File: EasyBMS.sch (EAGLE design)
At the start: 151 parts, among them IC1 LM2596S-5.0_NOPB, IC2 LTC6811IG-1#PBF, IC3 ESP32-S3-WROOM-1-N4R2, IC4 DRV103H, Q10 BSS84LT1G, Q11 BSS84LT1G, Q12 BSS84LT1G, Q13 BSS84LT1G, Q2 BSS84LT1G, Q3 BSS84LT1G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

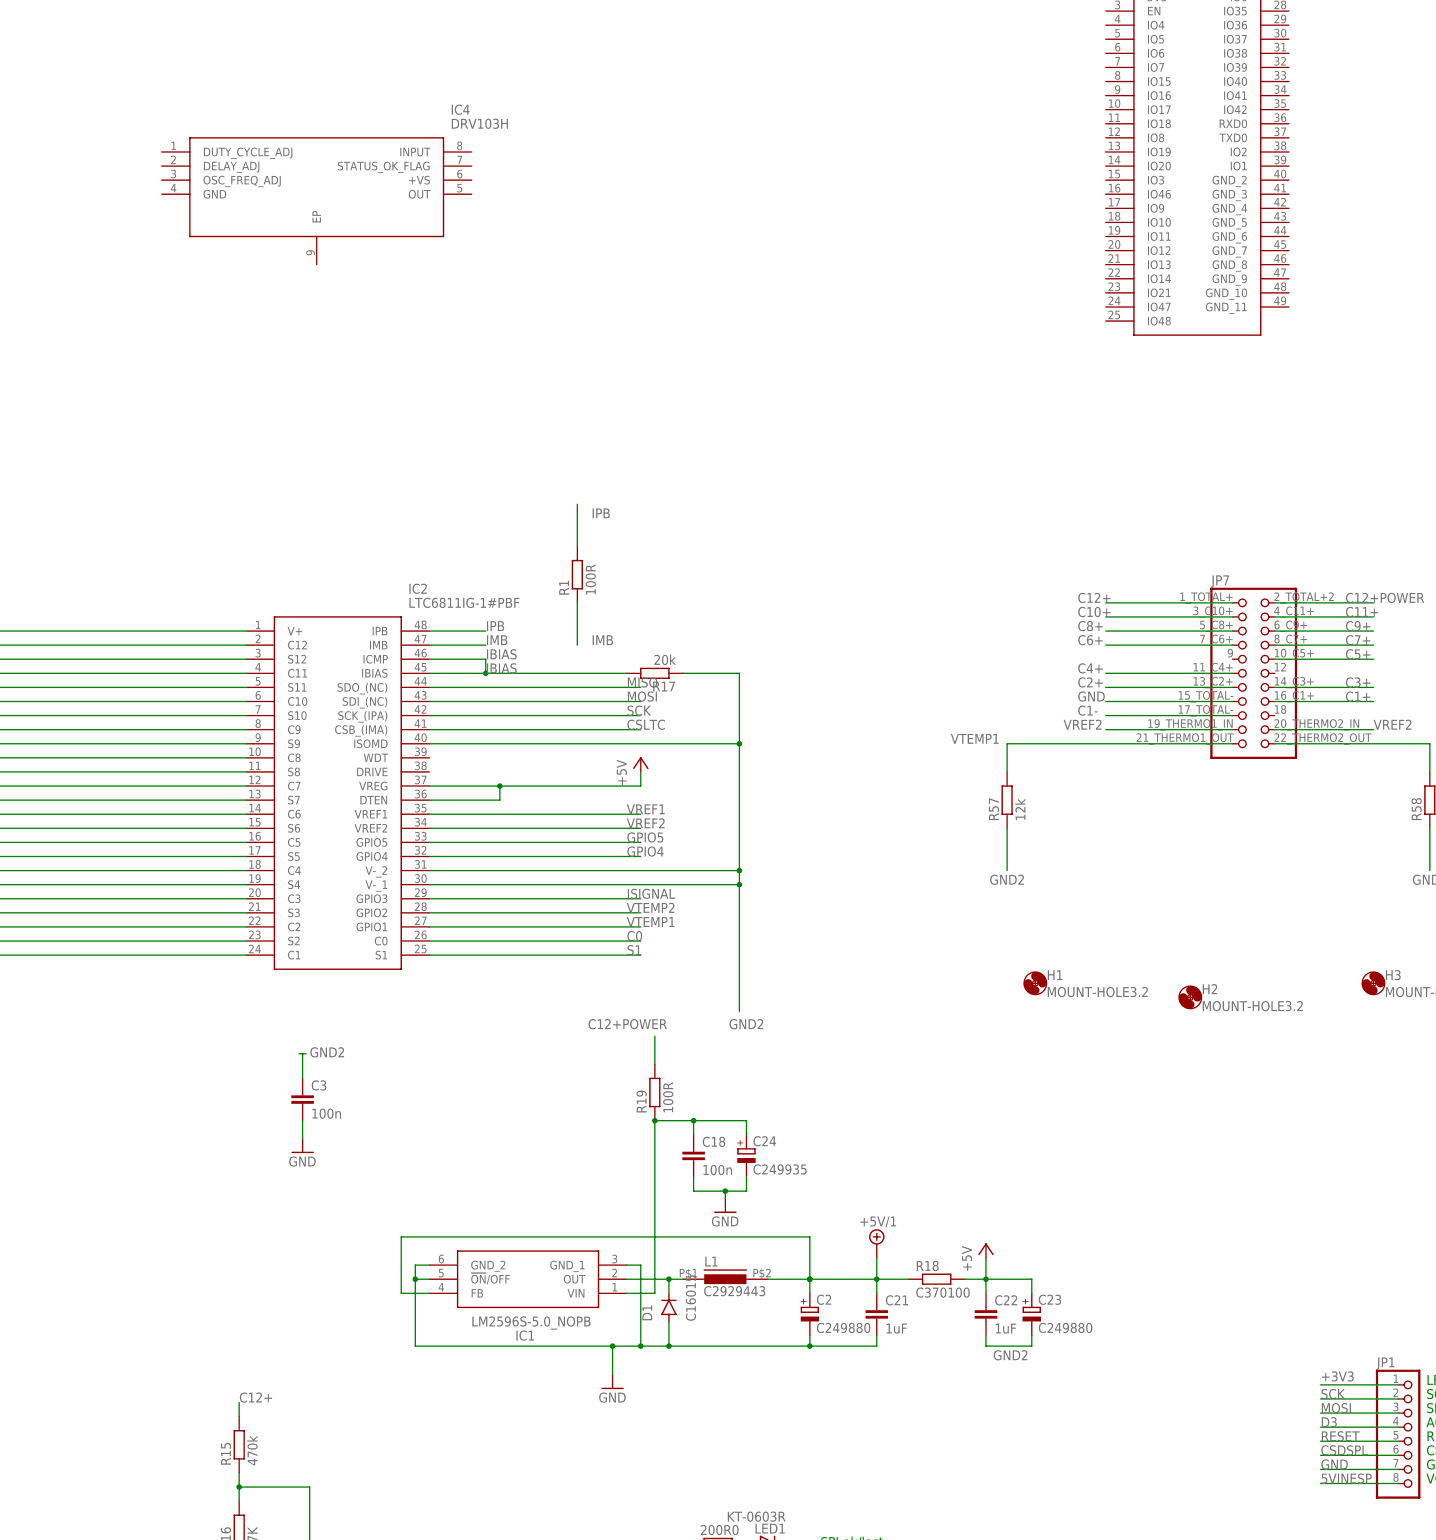
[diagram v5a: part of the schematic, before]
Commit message: new parts for DC DC added
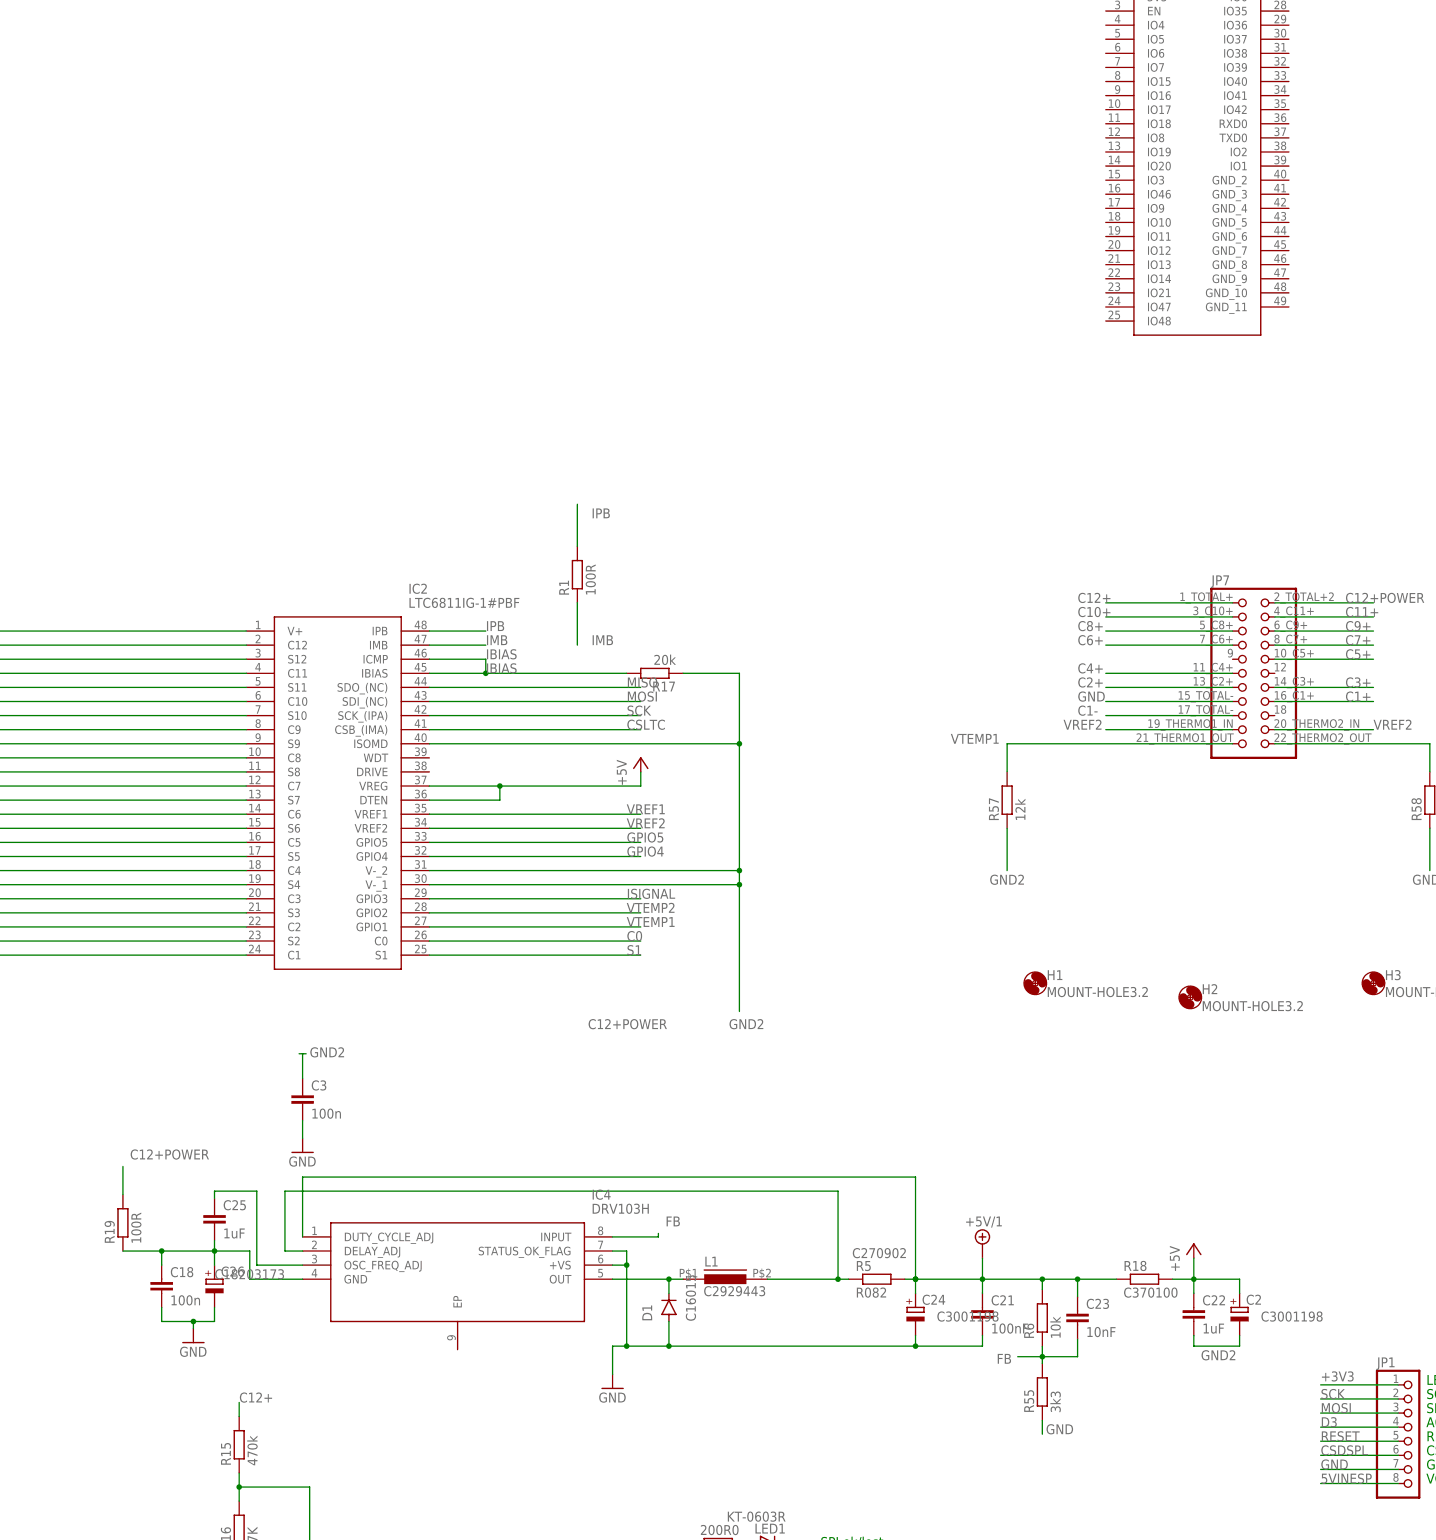
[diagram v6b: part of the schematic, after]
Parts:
- removed IC1: LM2596S-5.0_NOPB, SamacSys_Parts:LM2596S-5.0_NOPB
- added C25: 1uF, rcl:C-EUC1206
- added C26: (no value), rcl:CPOL-EU140CLH-0810
- added R5: R082, rcl:R-EU_R1206
- added R55: 3k3, rcl:R-EU_R0402
- added R6: 10k, rcl:R-EU_R0402
- C2: value C249880 -> (none); device rcl:CPOL-EUUD-8X10 -> rcl:CPOL-EU153CLV-0405; LCSC (none) -> C3001198
- C21: value 1uF -> 100nF; device rcl:C-EUC1206 -> rcl:C-EUC0805
- C23: value C249880 -> 10nF; device rcl:CPOL-EUUD-8X10 -> rcl:C-EUC0402
- C24: value C249935 -> (none); device SamacSys_Parts:VZH471M1JTR-1616 -> rcl:CPOL-EU153CLV-0405; LCSC (none) -> C3001198
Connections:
- new net FB: C23.2, IC4.INPUT, R55.2, R6.1
- new net N$3: C25.1, IC4.OSC_FREQ_ADJ
- new net N$5: IC4.DELAY_ADJ, L1.2, R5.1
- net +5V: now also C2.+; no longer C23.+
- net +5V/1: now also C23.1, C24.+, IC4.DUTY_CYCLE_ADJ, R5.2, R6.2; no longer C2.+, IC1.FB, L1.2
- net GND: now also C26.-, IC4.+VS, IC4.STATUS_OK_FLAG, R55.1; no longer C2.-, IC1.!ON!/OFF, IC1.GND_1, IC1.GND_2
- net GND2: now also C2.-; no longer C23.-
- net N$17: now also IC4.OUT; no longer IC1.OUT
- net N$75: now also C25.2, C26.+, IC4.GND; no longer C24.+, IC1.VIN
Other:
- moved on the sheet: C18, C2, C21, C22, C24, IC4, R18, R19

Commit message: XL7046 properly added
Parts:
- removed C23: 10nF, rcl:C-EUC0402
- removed C25: 1uF, rcl:C-EUC1206
- removed D1: C16015, diode:DIODE-DO214AC
- removed IC4: DRV103H, SamacSys_Parts:DRV103H
- added C27: 1uF, rcl:C-EUC1206
- added D3: C16015, diode:DIODE-DO214AC
- added IC1: XL7046, SamacSys_Parts:XL7046
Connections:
- removed net FB: C23.2, IC4.INPUT, R55.2, R6.1
- removed net N$17: D1.C, IC4.OUT, L1.1
- removed net N$3: C25.1, IC4.OSC_FREQ_ADJ
- removed net N$5: IC4.DELAY_ADJ, L1.2, R5.1
- removed net N$75: C18.1, C25.2, C26.+, IC4.GND, R19.1
- new net N$15: IC1.CSP, L1.2, R5.1
- new net N$25: IC1.FB, R55.2, R6.1
- new net N$6: C27.2, IC1.VC
- new net N$7: D3.C, IC1.SW, L1.1
- new net N$73: C18.1, C26.+, C27.1, IC1.VIN, R19.1
- net +5V/1: now also IC1.CSN; no longer C23.1, IC4.DUTY_CYCLE_ADJ
- net GND: now also D3.A, IC1.GND; no longer D1.A, IC4.+VS, IC4.STATUS_OK_FLAG
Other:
- note added: "LTC BMS Chip"
- note added: "Microcontroller"
- note added: "Pinheader für Display"
- moved on the sheet: C1, C18, C19, C2, C21, C22, C24, C26, C3, C4, D2, JP1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

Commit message: balancer path reworked2
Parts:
- removed U$2: WEMOS-D1-MINI, diy-modules:WEMOS-D1-MINI
- added C25, C29: 10nF, rcl:C-EUC0402
- added D4, D6: (no value), semicon-smd-ipc:D-MLL-34
- added Q14, Q16: C8547, SamacSys_Parts:BSS308PEH6327XTSA1
- added R103, R104, R82, R96: 10R0, rcl:R-EU_R1206
- added R105, R97: 3.3k, rcl:R-EU_R0402
- added R106, R98: 100R, rcl:R-EU_R0402
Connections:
- new net C: C25.1, C29.1, D4.C, D6.C, R106.1, R98.1
- new net LOWER: C25.2, C29.2, D4.A, D6.A, R103.1, R82.1
- new net N$18: R82.2, R96.1
- new net N$75: Q14.D, R96.2
- new net N$76: Q14.G, R97.2
- new net N$80: R103.2, R104.1
- new net N$81: Q16.D, R104.2
- new net N$82: Q16.G, R105.2
- new net S: R105.1, R97.1
- new net UPPER: Q14.S, Q16.S, R106.2, R98.2
- net +3V3: no longer U$2.3V3
- net 5VINESP: no longer U$2.5V
- net A0IN: no longer U$2.A0
- net CSDSPL: no longer U$2.D0
- net CSLTC: no longer U$2.D8
- net D3: no longer U$2.D3
- net GND: now also IC1.EN, IC1.EP; no longer U$2.GND
- net MISO: no longer U$2.D6
- net MOSI: no longer U$2.D7
- net N$124: no longer U$2.D2
- net N$30: no longer U$2.D4
- net N$70: no longer U$2.D1
- net RESET: no longer U$2.RST
- net SCK: no longer U$2.D5
